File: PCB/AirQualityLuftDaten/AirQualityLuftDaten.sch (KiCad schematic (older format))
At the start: 21 parts, among them J1 5V_DC_JACK, J10 I2C_2, J11 I2C_3, J12 DHT22, J13 SDS011, J14 ESP_BO1, J15 ESP_BO2, J16 LOGO_LUFTDATEN, J17 LOGO_AirRohr, J18 LOGO_TCEC, J2 5V_SCREW, J3 ADC_IN, J4 ADAFRUIT_ADS1115_ADC, J5 PCB, J6 LOGO_OSW, J7 LOGO_TCEC, J8 BME280, J9 I2C_1, P1 5V_USB_Micro, U1 NODEMCU

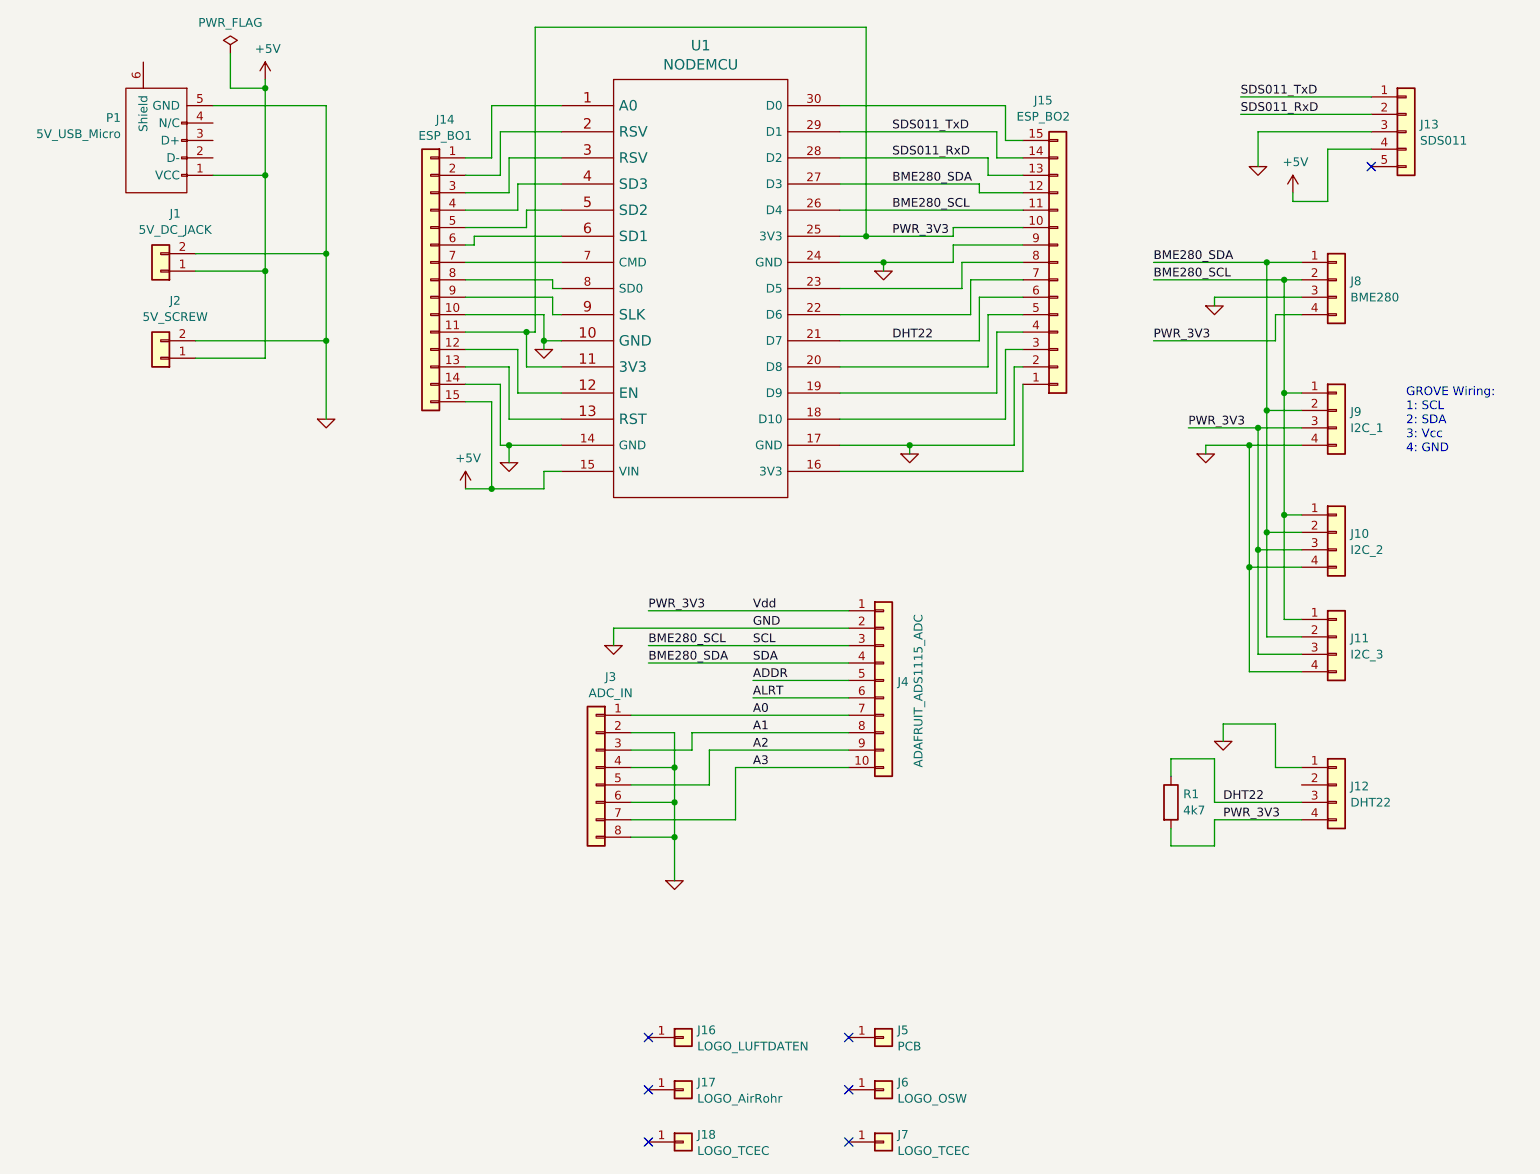
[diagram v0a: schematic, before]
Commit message: Updated PCB and baseplate files
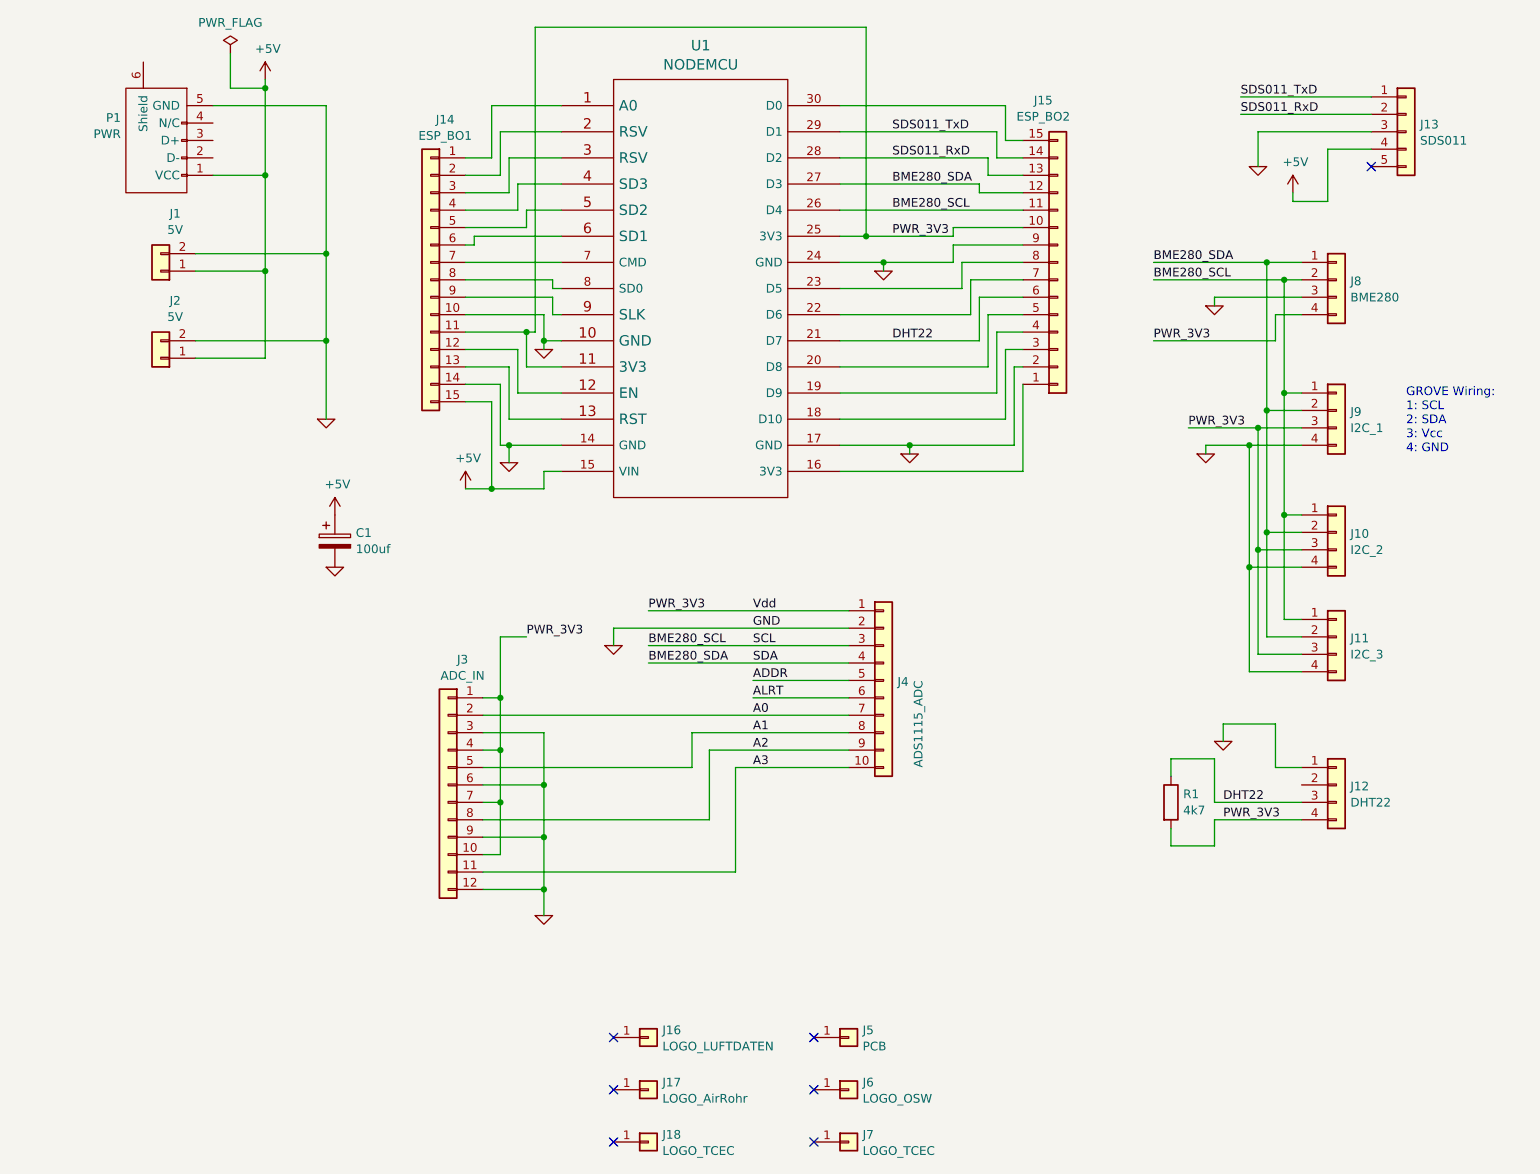
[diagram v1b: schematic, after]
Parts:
- removed J3: ADC_IN, REInnovationFootprint:SIL_8_Screw_AIO, symbol Connector_Generic:Conn_01x08
- added C1: 100uf, REInnovationFootprint:C_Radial_D6.3_L11.2_P2.5, symbol Device:CP
- added J3: ADC_IN, REInnovationFootprint:PinSocket_1x12_P2.54mm_Vertical_Labelled, symbol Connector_Generic:Conn_01x12
- J1: value 5V_DC_JACK -> 5V
- J16: footprint CuriousElectric3:2019_011_16_CuriousElectricCompany_Logo_Round_Logo_No_words_KiCAD_10mm_PCBLogo -> CuriousElectric3:sensorcommunity
- J17: footprint CuriousElectric3:2019_011_16_CuriousElectricCompany_Logo_Round_Logo_No_words_KiCAD_10mm_PCBLogo -> CuriousElectric3:logo_conversion
- J2: value 5V_SCREW -> 5V
- J4: value ADAFRUIT_ADS1115_ADC -> ADS1115_ADC
- P1: value 5V_USB_Micro -> PWR
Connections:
- net +5V: now also C1.1
- net A0: now also J3.2 (Pin_2)
- net A1: now also J3.5 (Pin_5)
- net A2: now also J3.8 (Pin_8)
- net A3: now also J3.11 (Pin_11)
- net GND: now also C1.2, J3.12 (Pin_12), J3.3 (Pin_3), J3.6 (Pin_6), J3.9 (Pin_9)
- net PWR_3V3: now also J3.1 (Pin_1), J3.10 (Pin_10), J3.4 (Pin_4), J3.7 (Pin_7)
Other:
- moved on the sheet: J16, J17, J18, J5, J6, J7
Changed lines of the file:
@@
 P 2100 2350
 F 0 "J1" H 2017 2020 50  0000 C CNN
-F 1 "5V_DC_JACK" H 2017 2113 50  0000 C CNN
+F 1 "5V" H 2017 2113 50  0000 C CNN
 F 2 "REInnovationFootprint:DC_Power_2_1" H 2100 2350 50  0001 C CNN
 F 3 "~" H 2100 2350 50  0001 C CNN
@@
 P 2100 2850
 F 0 "J2" H 2017 2520 50  0000 C CNN
-F 1 "5V_SCREW" H 2017 2613 50  0000 C CNN
+F 1 "5V" H 2017 2613 50  0000 C CNN
 F 2 "REInnovationFootprint:SIL-2_screw_terminal" H 2100 2850 50  0001 C CNN
 F 3 "~" H 2100 2850 50  0001 C CNN
@@
 P 2100 1600
 F 0 "P1" V 2230 1829 50  0000 L CNN
-F 1 "5V_USB_Micro" V 2137 1829 50  0000 L CNN
+F 1 "PWR" V 2137 1829 50  0000 L CNN
 F 2 "REInnovationFootprint:USB_Micro-B_MOLEX_47642-0001" V 2050 1500 50  0001 C CNN
 F 3 "" V 2050 1500 50  0000 C CNN
@@
 L Connector_Generic:Conn_01x01 J5
 U 1 1 5EE54DE8
-P 6250 6750
-F 0 "J5" H 6330 6792 50  0000 L CNN
-F 1 "PCB" H 6330 6699 50  0000 L CNN
-F 2 "REInnovationFootprint:PCB_LuftDaten_70x70" H 6250 6750 50  0001 C CNN
-F 3 "~" H 6250 6750 50  0001 C CNN
-	1    6250 6750
+P 6050 6750
+F 0 "J5" H 6130 6792 50  0000 L CNN
+F 1 "PCB" H 6130 6699 50  0000 L CNN
+F 2 "REInnovationFootprint:PCB_LuftDaten_70x70" H 6050 6750 50  0001 C CNN
+F 3 "~" H 6050 6750 50  0001 C CNN
+	1    6050 6750
 	1    0    0    -1
 $EndComp
@@
 L Connector_Generic:Conn_01x01 J6
 U 1 1 5EE56044
-P 6250 7050
-F 0 "J6" H 6330 7092 50  0000 L CNN
-F 1 "LOGO_OSW" H 6330 6999 50  0000 L CNN
-F 2 "REInnovationFootprint:OSHW_logo_small_back" H 6250 7050 50  0001 C CNN
-F 3 "~" H 6250 7050 50  0001 C CNN
-	1    6250 7050
+P 6050 7050
+F 0 "J6" H 6130 7092 50  0000 L CNN
+F 1 "LOGO_OSW" H 6130 6999 50  0000 L CNN
+F 2 "REInnovationFootprint:OSHW_logo_small_back" H 6050 7050 50  0001 C CNN
+F 3 "~" H 6050 7050 50  0001 C CNN
+	1    6050 7050
 	1    0    0    -1
 $EndComp
@@
 L Connector_Generic:Conn_01x01 J7
 U 1 1 5EE565C9
-P 6250 7350
-F 0 "J7" H 6330 7392 50  0000 L CNN
-F 1 "LOGO_TCEC" H 6330 7299 50  0000 L CNN
-F 2 "CuriousElectric3:TCEC_Words_13mm" H 6250 7350 50  0001 C CNN
-F 3 "~" H 6250 7350 50  0001 C CNN
-	1    6250 7350
-	1    0    0    -1
-$EndComp
-NoConn ~ 6050 6750
-NoConn ~ 6050 7050
-NoConn ~ 6050 7350
+P 6050 7350
+F 0 "J7" H 6130 7392 50  0000 L CNN
+F 1 "LOGO_TCEC" H 6130 7299 50  0000 L CNN
+F 2 "CuriousElectric3:TCEC_Words_13mm" H 6050 7350 50  0001 C CNN
+F 3 "~" H 6050 7350 50  0001 C CNN
+	1    6050 7350
+	1    0    0    -1
+$EndComp
+NoConn ~ 5850 6750
+NoConn ~ 5850 7050
+NoConn ~ 5850 7350
 $Comp
 L power:+5V #PWR013
@@
 P 6250 4700
 F 0 "J4" H 6330 4692 50  0000 L CNN
-F 1 "ADAFRUIT_ADS1115_ADC" V 6450 4200 50  0000 L CNN
+F 1 "ADS1115_ADC" V 6450 4200 50  0000 L CNN
 F 2 "REInnovationFootprint:ADAFRUIT_ADS1115" H 6250 4700 50  0001 C CNN
 F 3 "~" H 6250 4700 50  0001 C CNN
@@
 	4900 4600 6050 4600
 $Comp
-L Connector_Generic:Conn_01x08 J3
-U 1 1 5EF254B4
-P 4600 5200
-F 0 "J3" H 4517 5720 50  0000 C CNN
-F 1 "ADC_IN" H 4517 5627 50  0000 C CNN
-F 2 "REInnovationFootprint:SIL_8_Screw_AIO" H 4600 5200 50  0001 C CNN
-F 3 "~" H 4600 5200 50  0001 C CNN
-	1    4600 5200
-	-1   0    0    -1
-$EndComp
-$Comp
 L matts_components:GND #PWR07
 U 1 1 5EF2C87D
-P 5050 5850
-F 0 "#PWR07" H 5050 5850 30  0001 C CNN
-F 1 "GND" H 5050 5780 30  0001 C CNN
-F 2 "" H 5050 5850 60  0000 C CNN
-F 3 "" H 5050 5850 60  0000 C CNN
-	1    5050 5850
-	1    0    0    -1
-$EndComp
-Wire Wire Line
-	4800 4900 6050 4900
-Wire Wire Line
-	4800 5100 5150 5100
-Wire Wire Line
-	5150 5100 5150 5000
+P 4300 6050
+F 0 "#PWR07" H 4300 6050 30  0001 C CNN
+F 1 "GND" H 4300 5980 30  0001 C CNN
+F 2 "" H 4300 6050 60  0000 C CNN
+F 3 "" H 4300 6050 60  0000 C CNN
+	1    4300 6050
+	1    0    0    -1
+$EndComp
 Wire Wire Line
 	5150 5000 6050 5000
 Wire Wire Line
-	4800 5300 5250 5300
-Wire Wire Line
-	5250 5300 5250 5100
-Wire Wire Line
 	5250 5100 6050 5100
 Wire Wire Line
-	4800 5500 5400 5500
-Wire Wire Line
-	5400 5500 5400 5200
-Wire Wire Line
 	5400 5200 6050 5200
-Wire Wire Line
-	5050 5850 5050 5600
-Wire Wire Line
-	5050 5000 4800 5000
-Wire Wire Line
-	4800 5200 5050 5200
-Connection ~ 5050 5200
-Wire Wire Line
-	5050 5200 5050 5000
-Wire Wire Line
-	4800 5400 5050 5400
-Connection ~ 5050 5400
-Wire Wire Line
-	5050 5400 5050 5200
-Wire Wire Line
-	4800 5600 5050 5600
-Connection ~ 5050 5600
-Wire Wire Line
-	5050 5600 5050 5400
 Wire Wire Line
 	9050 1350 8300 1350
@@
 L Connector_Generic:Conn_01x01 J16
 U 1 1 5F00EC5C
-P 5100 6750
-F 0 "J16" H 5180 6792 50  0000 L CNN
-F 1 "LOGO_LUFTDATEN" H 5180 6699 50  0000 L CNN
-F 2 "CuriousElectric3:2019_011_16_CuriousElectricCompany_Logo_Round_Logo_No_words_KiCAD_10mm_PCBLogo" H 5100 6750 50  0001 C CNN
-F 3 "~" H 5100 6750 50  0001 C CNN
-	1    5100 6750
-	1    0    0    -1
-$EndComp
-NoConn ~ 4900 6750
+P 4900 6750
+F 0 "J16" H 4980 6792 50  0000 L CNN
+F 1 "LOGO_LUFTDATEN" H 4980 6699 50  0000 L CNN
+F 2 "CuriousElectric3:sensorcommunity" H 4900 6750 50  0001 C CNN
+F 3 "~" H 4900 6750 50  0001 C CNN
+	1    4900 6750
+	1    0    0    -1
+$EndComp
+NoConn ~ 4700 6750
 $Comp
 L Connector_Generic:Conn_01x01 J17
 U 1 1 5F019F93
-P 5100 7050
-F 0 "J17" H 5180 7092 50  0000 L CNN
-F 1 "LOGO_AirRohr" H 5180 6999 50  0000 L CNN
-F 2 "CuriousElectric3:2019_011_16_CuriousElectricCompany_Logo_Round_Logo_No_words_KiCAD_10mm_PCBLogo" H 5100 7050 50  0001 C CNN
-F 3 "~" H 5100 7050 50  0001 C CNN
-	1    5100 7050
-	1    0    0    -1
-$EndComp
-NoConn ~ 4900 7050
+P 4900 7050
+F 0 "J17" H 4980 7092 50  0000 L CNN
+F 1 "LOGO_AirRohr" H 4980 6999 50  0000 L CNN
+F 2 "CuriousElectric3:logo_conversion" H 4900 7050 50  0001 C CNN
+F 3 "~" H 4900 7050 50  0001 C CNN
+	1    4900 7050
+	1    0    0    -1
+$EndComp
+NoConn ~ 4700 7050
 $Comp
 L Connector_Generic:Conn_01x01 J18
 U 1 1 5F025232
-P 5100 7350
-F 0 "J18" H 5180 7392 50  0000 L CNN
-F 1 "LOGO_TCEC" H 5180 7299 50  0000 L CNN
-F 2 "CuriousElectric3:2019_011_16_CuriousElectricCompany_Logo_Round_Logo_No_words_KiCAD_10mm_PCBLogo" H 5100 7350 50  0001 C CNN
-F 3 "~" H 5100 7350 50  0001 C CNN
-	1    5100 7350
-	1    0    0    -1
-$EndComp
-NoConn ~ 4900 7350
+P 4900 7350
+F 0 "J18" H 4980 7392 50  0000 L CNN
+F 1 "LOGO_TCEC" H 4980 7299 50  0000 L CNN
+F 2 "CuriousElectric3:2019_011_16_CuriousElectricCompany_Logo_Round_Logo_No_words_KiCAD_10mm_PCBLogo" H 4900 7350 50  0001 C CNN
+F 3 "~" H 4900 7350 50  0001 C CNN
+	1    4900 7350
+	1    0    0    -1
+$EndComp
+NoConn ~ 4700 7350
+$Comp
+L power:+5V #PWR0101
+U 1 1 5EF1E4D2
+P 3100 3750
+F 0 "#PWR0101" H 3100 3600 50  0001 C CNN
+F 1 "+5V" H 3115 3926 50  0000 C CNN
+F 2 "" H 3100 3750 50  0001 C CNN
+F 3 "" H 3100 3750 50  0001 C CNN
+	1    3100 3750
+	1    0    0    -1
+$EndComp
+$Comp
+L matts_components:GND #PWR0102
+U 1 1 5EF1E8E5
+P 3100 4050
+F 0 "#PWR0102" H 3100 4050 30  0001 C CNN
+F 1 "GND" H 3100 3980 30  0001 C CNN
+F 2 "" H 3100 4050 60  0000 C CNN
+F 3 "" H 3100 4050 60  0000 C CNN
+	1    3100 4050
+	1    0    0    -1
+$EndComp
+$Comp
+L Device:CP C1
+U 1 1 5EF1F0DE
+P 3100 3900
+F 0 "C1" H 3220 3947 50  0000 L CNN
+F 1 "100uf" H 3220 3854 50  0000 L CNN
+F 2 "REInnovationFootprint:C_Radial_D6.3_L11.2_P2.5" H 3138 3750 50  0001 C CNN
+F 3 "~" H 3100 3900 50  0001 C CNN
+	1    3100 3900
+	1    0    0    -1
+$EndComp
+Text Label 4200 4450 0    50   ~ 0
+PWR_3V3
+$Comp
+L Connector_Generic:Conn_01x12 J3
+U 1 1 5F13C6F2
+P 3750 5300
+F 0 "J3" H 3667 6020 50  0000 C CNN
+F 1 "ADC_IN" H 3667 5927 50  0000 C CNN
+F 2 "REInnovationFootprint:PinSocket_1x12_P2.54mm_Vertical_Labelled" H 3750 5300 50  0001 C CNN
+F 3 "~" H 3750 5300 50  0001 C CNN
+	1    3750 5300
+	-1   0    0    -1
+$EndComp
+Wire Wire Line
+	5400 5200 5400 5800
+Wire Wire Line
+	5250 5100 5250 5500
+Wire Wire Line
+	5150 5000 5150 5200
+Wire Wire Line
+	3950 5200 5150 5200
+Wire Wire Line
+	3950 4900 6050 4900
+Wire Wire Line
+	3950 5500 5250 5500
+Wire Wire Line
+	3950 5800 5400 5800
+Wire Wire Line
+	4300 6050 4300 5900
+Wire Wire Line
+	4300 5000 3950 5000
+Wire Wire Line
+	3950 5300 4300 5300
+Connection ~ 4300 5300
+Wire Wire Line
+	4300 5300 4300 5000
+Wire Wire Line
+	3950 5600 4300 5600
+Connection ~ 4300 5600
+Wire Wire Line
+	4300 5600 4300 5300
+Wire Wire Line
+	3950 5900 4300 5900
+Connection ~ 4300 5900
+Wire Wire Line
+	4300 5900 4300 5600
+Wire Wire Line
+	3950 5700 4050 5700
+Wire Wire Line
+	4050 5700 4050 5400
+Wire Wire Line
+	4050 4450 4200 4450
+Wire Wire Line
+	3950 4800 4050 4800
+Connection ~ 4050 4800
+Wire Wire Line
+	4050 4800 4050 4450
+Wire Wire Line
+	3950 5100 4050 5100
+Connection ~ 4050 5100
+Wire Wire Line
+	4050 5100 4050 4800
+Wire Wire Line
+	3950 5400 4050 5400
+Connection ~ 4050 5400
+Wire Wire Line
+	4050 5400 4050 5100
 $EndSCHEMATC
